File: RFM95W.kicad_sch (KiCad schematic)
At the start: 3 parts, among them U7 RFM95W-915S2

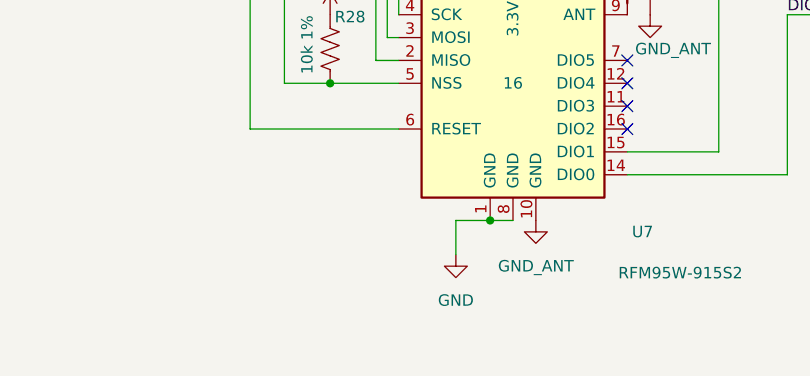
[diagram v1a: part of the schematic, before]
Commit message: added gnd-radio and gnd-ant zones on two layers. ERC and DRC mostly good. (Two warnings about pads field in NetTie footprints.)
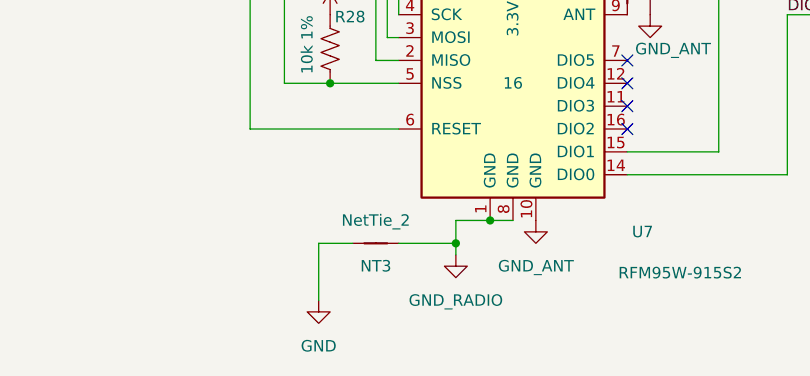
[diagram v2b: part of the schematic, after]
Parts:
- added NT3: NetTie_2, ProjectLib:NetTie-2_SMD_Pad0.5mm, symbol ProjectLib:NetTie_2
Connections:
- net GND: now also NT3.1; no longer U7.1 (GND), U7.8 (GND)
- new net GND_RADIO: NT3.2, U7.1 (GND), U7.8 (GND)
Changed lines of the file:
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@@
+	)
+	(junction
+		(at 109.22 102.87)
+		(diameter 0)
+		(color 0 0 0 0)
 	)
 	(junction
@@
 	(wire
 		(pts
+			(xy 97.79 102.87) (xy 93.98 102.87)
+		)
+		(stroke
+			(width 0)
+			(type default)
+		)
+	)
+	(wire
+		(pts
 			(xy 152.4 77.47) (xy 146.05 77.47)
 		)
@@
 	(wire
 		(pts
-			(xy 109.22 100.33) (xy 109.22 104.14)
+			(xy 109.22 102.87) (xy 109.22 104.14)
 		)
 		(stroke
@@
 	(wire
 		(pts
+			(xy 109.22 100.33) (xy 109.22 102.87)
+		)
+		(stroke
+			(width 0)
+			(type default)
+		)
+	)
+	(wire
+		(pts
 			(xy 138.43 73.66) (xy 138.43 92.71)
 		)
@@
 		)
 	)
+	(wire
+		(pts
+			(xy 102.87 102.87) (xy 109.22 102.87)
+		)
+		(stroke
+			(width 0)
+			(type default)
+		)
+	)
 	(bus
 		(pts
 			(xy 154.94 63.5) (xy 154.94 76.2)
+		)
+		(stroke
+			(width 0)
+			(type default)
+		)
+	)
+	(wire
+		(pts
+			(xy 93.98 102.87) (xy 93.98 109.22)
 		)
 		(stroke
@@
 	(symbol
 		(lib_id "power:GND")
+		(at 93.98 109.22 0)
+		(unit 1)
+		(body_style 1)
+		(exclude_from_sim no)
+		(in_bom yes)
+		(on_board yes)
+		(in_pos_files yes)
+		(dnp no)
+		(fields_autoplaced yes)
+		(property "Reference" "#PWR049"
+			(at 93.98 115.57 0)
+			(hide yes)
+			(show_name no)
+			(do_not_autoplace no)
+			(effects
+				(font
+					(size 1.27 1.27)
+				)
+			)
+		)
+		(property "Value" "GND"
+			(at 93.98 114.3 0)
+			(show_name no)
+			(do_not_autoplace no)
+			(effects
+				(font
+					(size 1.27 1.27)
+				)
+			)
+		)
+		(property "Footprint" ""
+			(at 93.98 109.22 0)
+			(hide yes)
+			(show_name no)
+			(do_not_autoplace no)
+			(effects
+				(font
+					(size 1.27 1.27)
+				)
+			)
+		)
+		(property "Datasheet" ""
+			(at 93.98 109.22 0)
+			(hide yes)
+			(show_name no)
+			(do_not_autoplace no)
+			(effects
+				(font
+					(size 1.27 1.27)
+				)
+			)
+		)
+		(property "Description" "Power symbol creates a global label with name \"GND\" , ground"
+			(at 93.98 109.22 0)
+			(hide yes)
+			(show_name no)
+			(do_not_autoplace no)
+			(effects
+				(font
+					(size 1.27 1.27)
+				)
+			)
+		)
+		(pin "1"
+		)
+		(instances
+			(project "SensorProject_t16-pcb"
+				(path "/0c2d0c14-8850-4a30-bb78-b2f40cb442ba/2db29b35-1005-45eb-b852-0b853354466f"
+					(reference "#PWR049")
+					(unit 1)
+				)
+			)
+		)
+	)
+	(symbol
+		(lib_id "power:GND")
 		(at 109.22 104.14 0)
 		(unit 1)
@@
 			)
 		)
-		(property "Value" "GND"
+		(property "Value" "GND_RADIO"
 			(at 109.22 109.22 0)
 			(show_name no)
@@
 					(unit 1)
 				)
+			)
+		)
+	)
+	(symbol
+		(lib_id "ProjectLib:NetTie_2")
+		(at 100.33 102.87 0)
+		(unit 1)
+		(body_style 1)
+		(exclude_from_sim no)
+		(in_bom no)
+		(on_board yes)
+		(in_pos_files no)
+		(dnp no)
+		(property "Reference" "NT3"
+			(at 100.33 105.41 0)
+			(show_name no)
+			(do_not_autoplace no)
+			(effects
+				(font
+					(size 1.27 1.27)
+				)
+			)
+		)
+		(property "Value" "NetTie_2"
+			(at 100.33 100.33 0)
+			(show_name no)
+			(do_not_autoplace no)
+			(effects
+				(font
+					(size 1.27 1.27)
+				)
+			)
+		)
+		(property "Footprint" "ProjectLib:NetTie-2_SMD_Pad0.5mm"
+			(at 100.33 102.87 0)
+			(hide yes)
+			(show_name no)
+			(do_not_autoplace no)
+			(effects
+				(font
+					(size 1.27 1.27)
+				)
+			)
+		)
+		(property "Datasheet" ""
+			(at 100.33 102.87 0)
+			(hide yes)
+			(show_name no)
+			(do_not_autoplace no)
+			(effects
+				(font
+					(size 1.27 1.27)
+				)
+			)
+		)
+		(property "Description" "Net tie, 2 pins"
+			(at 100.33 102.87 0)
+			(hide yes)
+			(show_name no)
+			(do_not_autoplace no)
+			(effects
+				(font
+					(size 1.27 1.27)
+				)
+			)
+		)
+		(property "pads" "2"
+			(at 100.33 102.87 0)
+			(hide yes)
+			(show_name no)
+			(do_not_autoplace no)
+			(effects
+				(font
+					(size 1.27 1.27)
+				)
+			)
+		)
+		(pin "2"
+		)
+		(pin "1"
+		)
+		(instances
+			(project "SensorProject_t16-pcb"
+				(path "/0c2d0c14-8850-4a30-bb78-b2f40cb442ba/2db29b35-1005-45eb-b852-0b853354466f"
+					(reference "NT3")
+					(unit 1)
+				)

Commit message: added caps to radio_gnd.
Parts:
- added C18: 10uF, ProjectLib:C_0402_1005Metric, symbol ProjectLib:C
- added C19: 100nF, ProjectLib:C_0402_1005Metric, symbol ProjectLib:C
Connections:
- net +3V3: now also C18.1, C19.1
- net GND_RADIO: now also C18.2, C19.2
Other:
- moved on the sheet: R28

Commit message: Cleaned up v0.3.0 2026-04. LSE and HSE populated.
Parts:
- C18: Notes (none) -> or equivalent; Package (none) -> C_0402_1005Metric
- C19: Manufacturer Yageo -> (none); MfgPart CC0402KRX7R7BB104 -> (none); Notes (none) -> or equivalent; Package (none) -> C_0402_1005Metric
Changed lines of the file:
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@@
 			)
 		)
-		(property "Manufacturer" "Yageo"
+		(property "Manufacturer" ""
 			(at 100.33 62.23 0)
 			(hide yes)
@@
 			)
 		)
-		(property "MfgPart" "CC0402KRX7R7BB104"
+		(property "MfgPart" ""
+			(at 100.33 62.23 0)
+			(hide yes)
+			(show_name no)
+			(do_not_autoplace no)
+			(effects
+				(font
+					(size 1.27 1.27)
+				)
+			)
+		)
+		(property "Notes" "or equivalent"
+			(at 100.33 62.23 0)
+			(hide yes)
+			(show_name no)
+			(do_not_autoplace no)
+			(effects
+				(font
+					(size 1.27 1.27)
+				)
+			)
+		)
+		(property "Package" "C_0402_1005Metric"
 			(at 100.33 62.23 0)
 			(hide yes)
@@
 			(at 106.68 62.23 0)
 			(hide yes)
+			(show_name no)
+			(do_not_autoplace no)
+			(effects
+				(font
+					(size 1.27 1.27)
+				)
+			)
+		)
+		(property "Notes" "or equivalent"
+			(at 106.68 62.23 0)
+			(hide yes)
+			(show_name no)
+			(do_not_autoplace no)
+			(effects
+				(font
+					(size 1.27 1.27)
+				)
+			)
+		)
+		(property "Package" "C_0402_1005Metric"
+			(at 106.68 62.23 0)
+			(hide yes)

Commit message: added QR and ID blocks on silkscreen. Marked HSE and LSE as DNP. Revised version number to 0.3.1.
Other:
- title: RFM95W 915MHz -> stm32f411, RFM95W
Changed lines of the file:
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@@
 	(paper "A4")
 	(title_block
-		(title "RFM95W 915MHz")
-		(date "2025-09-15")
-		(rev "v0.2.2")
+		(title "stm32f411, RFM95W")
+		(date "2026-04-12")
+		(rev "v0.3.1")
 	)
 	(junction
